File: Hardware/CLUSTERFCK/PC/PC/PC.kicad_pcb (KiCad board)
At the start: 2 copper layers, 142.1 x 74 mm, 35 parts, among them J1 Conn_02x20_Counter_Clockwise, U1 74LS245, U2 74LS161, U3 74LS245, U4 74LS161, U5 74LS161

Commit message: 0042 | 6h | Layout PC
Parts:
- moved D1 30.5 mm to (114.2, 60.4)
- moved D10 30.5 mm to (45.6, 60.4)
- moved D11 30.5 mm to (38.0, 60.4)
- moved D12 30.5 mm to (30.3, 60.4)
- moved D2 30.5 mm to (106.5, 60.4)
- moved D3 30.5 mm to (98.9, 60.4)
- moved D4 30.5 mm to (91.3, 60.4)
- moved D5 30.5 mm to (83.7, 60.4)
- moved D6 30.5 mm to (76.1, 60.4)
- moved D7 30.5 mm to (68.4, 60.4)
- moved D8 30.5 mm to (60.8, 60.4)
- moved D9 30.5 mm to (53.2, 60.4)
- moved R1 30.5 mm to (114.2, 53.4)
- moved R10 30.5 mm to (45.6, 53.4)
- moved R11 30.5 mm to (38.0, 53.4)
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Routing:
- net +5V: track 45.0 -> 302.7 mm, vias 0 -> 6
- net ~PO: track 0.00 -> 124.9 mm, vias 0 -> 5
- net CE: track 0.00 -> 110.8 mm, vias 0 -> 2
- net ~J: track 17.5 -> 122.0 mm, vias 2 -> 7
- net /ADDR1: track 26.4 -> 130.8 mm, vias 2 -> 4
- net /ADDR3: track 30.3 -> 133.9 mm, vias 2 -> 4
- net /ADDR2: track 27.9 -> 129.3 mm, vias 2 -> 4
- net /ADDR0: track 24.9 -> 126.1 mm, vias 2 -> 4
- net CLK: track 0.00 -> 98.8 mm, vias 0 -> 3
- net /ADDR11: track 35.1 -> 110.3 mm, vias 2 -> 6
- net /ADDR9: track 32.2 -> 107.1 mm, vias 2 -> 6
- net /ADDR10: track 33.6 -> 105.6 mm, vias 2 -> 6
- net /ADDR8: track 30.7 -> 102.4 mm, vias 2 -> 6
- net /ADDR7: track 37.4 -> 104.0 mm, vias 2 -> 5
- net /ADDR5: track 34.5 -> 100.9 mm, vias 2 -> 5
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- added copper zone on B.Cu, net GND
- added copper zone on F.Cu, net GND
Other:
- board size 142.1 x 74 mm -> 142.1 x 63 mm

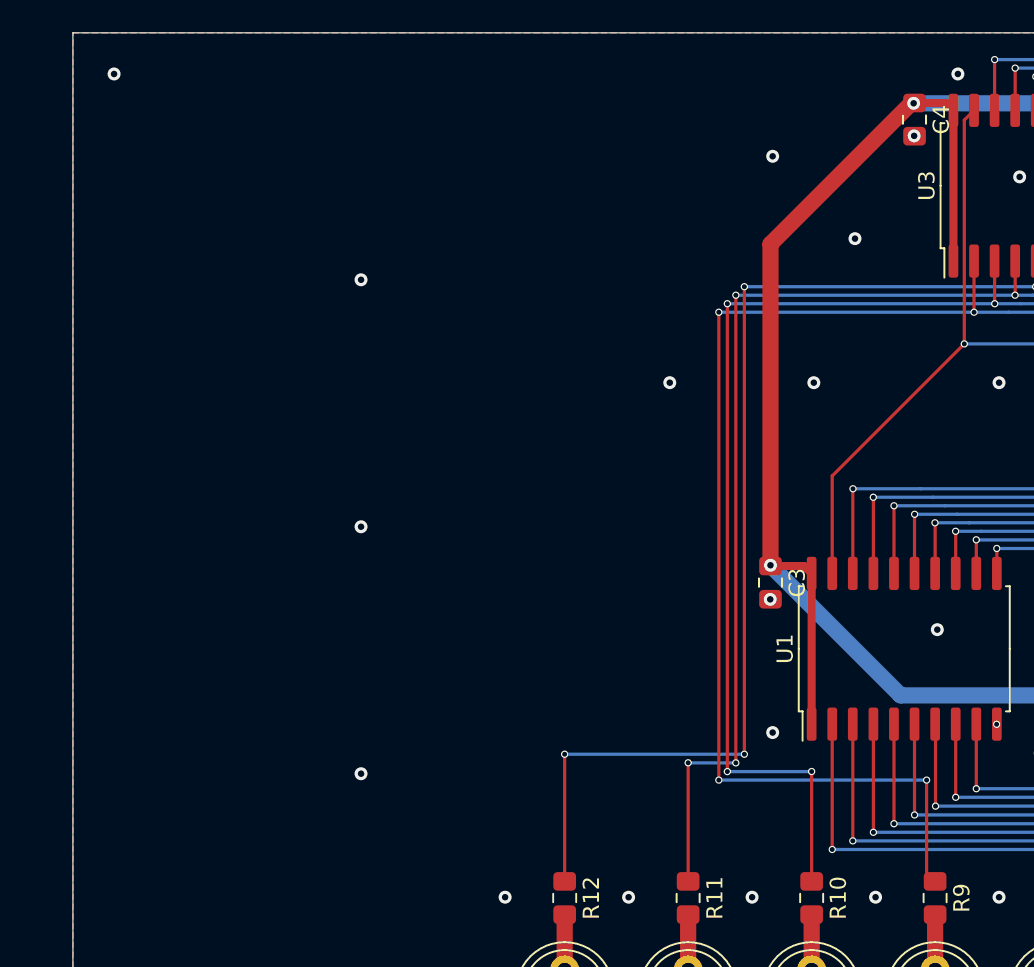
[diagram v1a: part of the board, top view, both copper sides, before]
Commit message: quickfix PC silkscreen
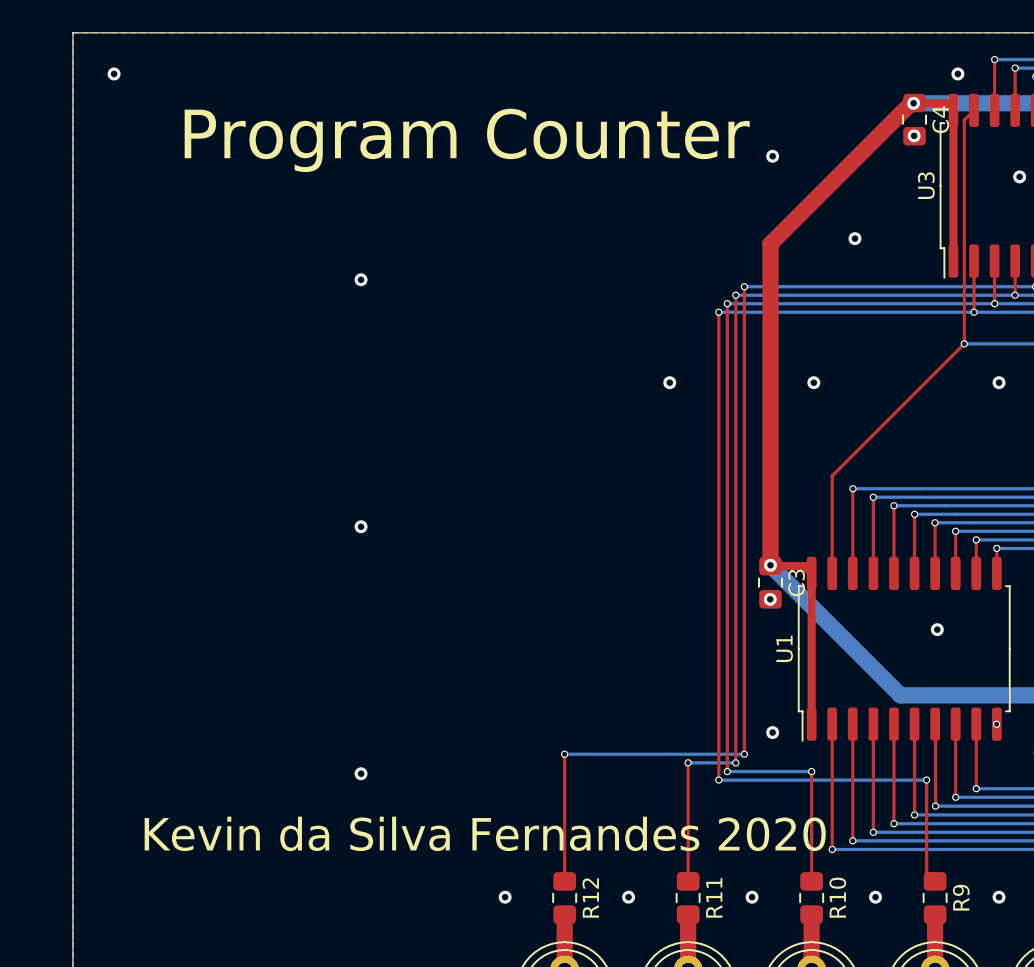
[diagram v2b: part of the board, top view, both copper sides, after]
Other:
- board text added: "Kevin da Silva Fernandes 2020"
- board text added: "Program Counter"
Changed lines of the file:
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@@
   (general
     (thickness 1.6)
-    (drawings 4)
+    (drawings 6)
     (tracks 542)
     (modules 35)
@@
       (dielectric_constraints no)
     )
-    (last_trace_width 0.2)
+    (last_trace_width 0.25)
     (user_trace_width 0.2)
     (user_trace_width 0.5)
@@
     )
   )
+  (gr_text "Kevin da Silva Fernandes 2020" (at 25.4 49.53) (layer "F.SilkS")
+    (effects (font (size 2 2) (thickness 0.3)))
+  )
+  (gr_text "Program Counter" (at 24.13 6.35) (layer "F.SilkS")
+    (effects (font (size 3 3) (thickness 0.7)))
+  )
   (gr_line (start 0 0) (end 0 63) (layer "Edge.Cuts") (width 0.05))
